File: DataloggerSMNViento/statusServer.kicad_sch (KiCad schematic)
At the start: 15 parts

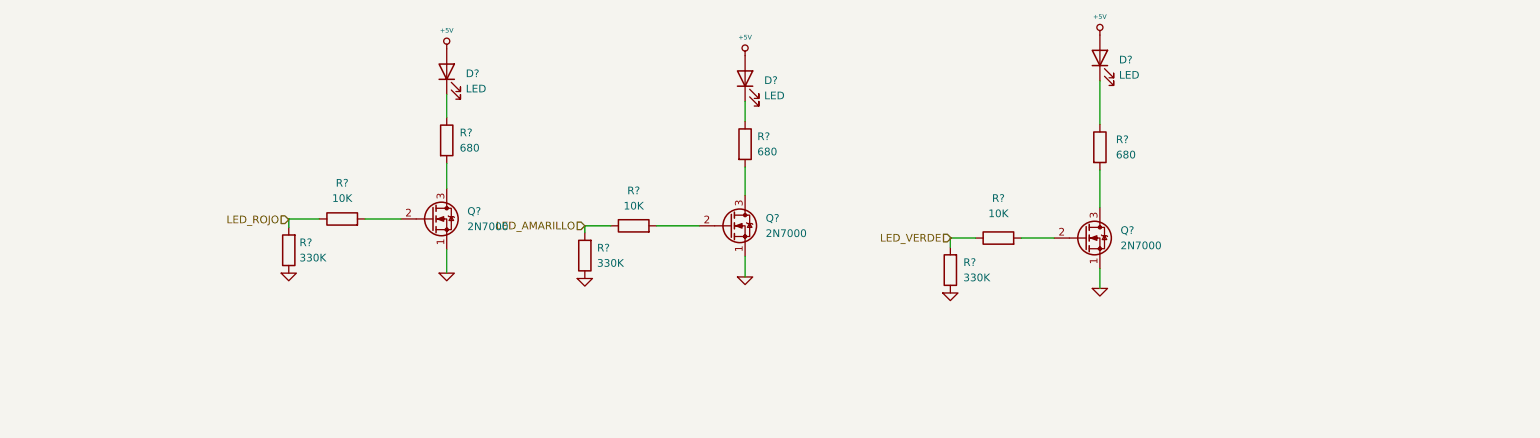
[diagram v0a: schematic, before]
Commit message: Agrego modificaciones al poncho de la EDU CIAA, también agrego una simulacion del circuito para tomar la tensión del ADC del tunnel
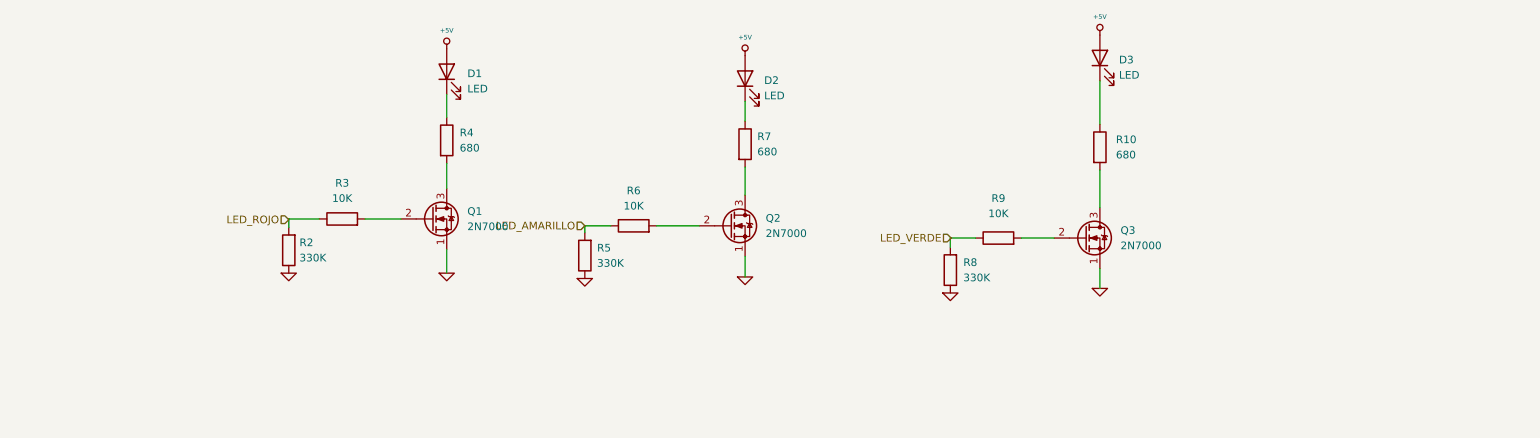
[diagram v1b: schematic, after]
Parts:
- D1, D2, D3: renamed from D?; footprint (none) -> LED_THT:LED_D3.0mm
- R10, R2, R3, R4, R5, R6, R7, R8, R9: renamed from R?; footprint (none) -> Resistor_THT:R_Axial_DIN0207_L6.3mm_D2.5mm_P15.24mm_Horizontal
- gave numbers to parts that had none: 3
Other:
- company: (none) -> Servicio Meteorológico Nacional - FIUBA - UBA
- title: (none) -> Datalogger para SCTV

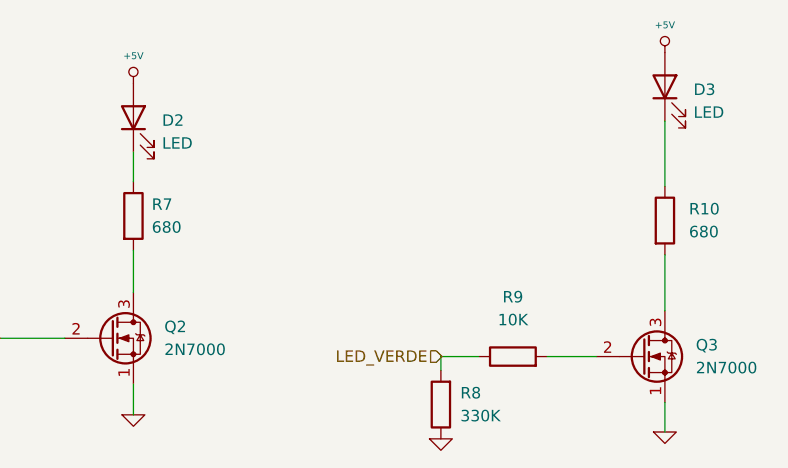
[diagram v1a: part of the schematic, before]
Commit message: Subo la version v1.0 del PCB del poncho de la tesis
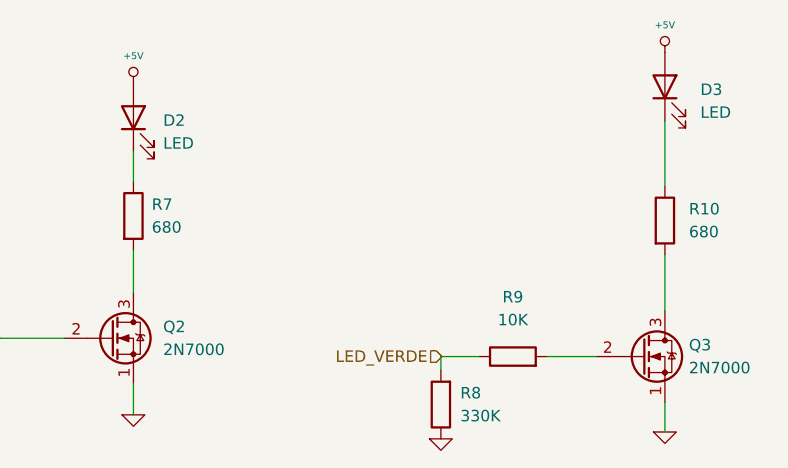
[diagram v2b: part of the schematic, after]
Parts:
- D1, D2, D3: footprint LED_THT:LED_D3.0mm -> LED_SMD:LED_1206_3216Metric
- Q1, Q2, Q3: footprint Package_TO_SOT_THT:TO-92_Inline -> Package_TO_SOT_SMD:SOT-23
- R10, R2, R3, R4, R5, R6, R7, R8, R9: footprint Resistor_THT:R_Axial_DIN0207_L6.3mm_D2.5mm_P15.24mm_Horizontal -> Resistor_SMD:R_1206_3216Metric
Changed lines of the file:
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@@
       (effects (font (size 1.27 1.27)) (justify left))
     )
-    (property "Footprint" "Package_TO_SOT_THT:TO-92_Inline" (id 2) (at 96.901 58.674 0)
+    (property "Footprint" "Package_TO_SOT_SMD:SOT-23" (id 2) (at 96.901 58.674 0)
       (effects (font (size 1.27 1.27) italic) (justify left) hide)
     )
@@
       (effects (font (size 1.27 1.27)) (justify right))
     )
-    (property "Footprint" "Resistor_THT:R_Axial_DIN0207_L6.3mm_D2.5mm_P15.24mm_Horizontal" (id 2) (at 179.959 65.278 90)
+    (property "Footprint" "Resistor_SMD:R_1206_3216Metric" (id 2) (at 179.959 65.278 90)
       (effects (font (size 1.27 1.27)) hide)
     )
@@
       (effects (font (size 1.27 1.27)) (justify left))
     )
-    (property "Footprint" "Resistor_THT:R_Axial_DIN0207_L6.3mm_D2.5mm_P15.24mm_Horizontal" (id 2) (at 201.295 44.831 90)
+    (property "Footprint" "Resistor_SMD:R_1206_3216Metric" (id 2) (at 201.295 44.831 90)
       (effects (font (size 1.27 1.27)) hide)
     )
@@
   (symbol (lib_id "Device:LED") (at 203.073 29.972 90) (unit 1)
     (in_bom yes) (on_board yes) (fields_autoplaced)
-    (property "Reference" "D3" (id 0) (at 206.248 30.2894 90)
-      (effects (font (size 1.27 1.27)) (justify right))
-    )
-    (property "Value" "LED" (id 1) (at 206.248 32.8294 90)
-      (effects (font (size 1.27 1.27)) (justify right))
-    )
-    (property "Footprint" "LED_THT:LED_D3.0mm" (id 2) (at 203.073 29.972 0)
+    (property "Reference" "D3" (id 0) (at 207.01 30.2894 90)
+      (effects (font (size 1.27 1.27)) (justify right))
+    )
+    (property "Value" "LED" (id 1) (at 207.01 32.8294 90)
+      (effects (font (size 1.27 1.27)) (justify right))
+    )
+    (property "Footprint" "LED_SMD:LED_1206_3216Metric" (id 2) (at 203.073 29.972 0)
       (effects (font (size 1.27 1.27)) hide)
     )
@@
       (effects (font (size 1.27 1.27)) (justify left))
     )
-    (property "Footprint" "Resistor_THT:R_Axial_DIN0207_L6.3mm_D2.5mm_P15.24mm_Horizontal" (id 2) (at 142.24 44.323 90)
+    (property "Footprint" "Resistor_SMD:R_1206_3216Metric" (id 2) (at 142.24 44.323 90)
       (effects (font (size 1.27 1.27)) hide)
     )
@@
       (effects (font (size 1.27 1.27)) (justify right))
     )
-    (property "Footprint" "LED_THT:LED_D3.0mm" (id 2) (at 94.361 32.258 0)
+    (property "Footprint" "LED_SMD:LED_1206_3216Metric" (id 2) (at 94.361 32.258 0)
       (effects (font (size 1.27 1.27)) hide)
     )
@@
     (property "Reference" "R3" (id 0) (at 76.962 50.8 90))
     (property "Value" "10K" (id 1) (at 76.962 53.34 90))
-    (property "Footprint" "Resistor_THT:R_Axial_DIN0207_L6.3mm_D2.5mm_P15.24mm_Horizontal" (id 2) (at 76.962 58.547 90)
+    (property "Footprint" "Resistor_SMD:R_1206_3216Metric" (id 2) (at 76.962 58.547 90)
       (effects (font (size 1.27 1.27)) hide)
     )
@@
   (symbol (lib_id "Transistor_FET:2N7000") (at 200.533 59.944 0) (unit 1)
     (in_bom yes) (on_board yes) (fields_autoplaced)
-    (property "Reference" "Q3" (id 0) (at 206.502 58.6739 0)
-      (effects (font (size 1.27 1.27)) (justify left))
-    )
-    (property "Value" "2N7000" (id 1) (at 206.502 61.2139 0)
-      (effects (font (size 1.27 1.27)) (justify left))
-    )
-    (property "Footprint" "Package_TO_SOT_THT:TO-92_Inline" (id 2) (at 205.613 61.849 0)
+    (property "Reference" "Q3" (id 0) (at 205.74 58.6739 0)
+      (effects (font (size 1.27 1.27)) (justify left))
+    )
+    (property "Value" "2N7000" (id 1) (at 205.74 61.2139 0)
+      (effects (font (size 1.27 1.27)) (justify left))
+    )
+    (property "Footprint" "Package_TO_SOT_SMD:SOT-23" (id 2) (at 205.613 61.849 0)
       (effects (font (size 1.27 1.27) italic) (justify left) hide)
     )
@@
       (effects (font (size 1.27 1.27)) (justify right))
     )
-    (property "Footprint" "Resistor_THT:R_Axial_DIN0207_L6.3mm_D2.5mm_P15.24mm_Horizontal" (id 2) (at 119.126 62.865 90)
+    (property "Footprint" "Resistor_SMD:R_1206_3216Metric" (id 2) (at 119.126 62.865 90)
       (effects (font (size 1.27 1.27)) hide)
     )
@@
     (property "Reference" "R6" (id 0) (at 125.476 52.07 90))
     (property "Value" "10K" (id 1) (at 125.476 54.61 90))
-    (property "Footprint" "Resistor_THT:R_Axial_DIN0207_L6.3mm_D2.5mm_P15.24mm_Horizontal" (id 2) (at 125.476 59.69 90)
+    (property "Footprint" "Resistor_SMD:R_1206_3216Metric" (id 2) (at 125.476 59.69 90)
       (effects (font (size 1.27 1.27)) hide)
     )
@@
   (symbol (lib_id "Transistor_FET:2N7000") (at 141.478 57.912 0) (unit 1)
     (in_bom yes) (on_board yes) (fields_autoplaced)
-    (property "Reference" "Q2" (id 0) (at 147.447 56.6419 0)
-      (effects (font (size 1.27 1.27)) (justify left))
-    )
-    (property "Value" "2N7000" (id 1) (at 147.447 59.1819 0)
-      (effects (font (size 1.27 1.27)) (justify left))
-    )
-    (property "Footprint" "Package_TO_SOT_THT:TO-92_Inline" (id 2) (at 146.558 59.817 0)
+    (property "Reference" "Q2" (id 0) (at 147.32 56.6419 0)
+      (effects (font (size 1.27 1.27)) (justify left))
+    )
+    (property "Value" "2N7000" (id 1) (at 147.32 59.1819 0)
+      (effects (font (size 1.27 1.27)) (justify left))
+    )
+    (property "Footprint" "Package_TO_SOT_SMD:SOT-23" (id 2) (at 146.558 59.817 0)
       (effects (font (size 1.27 1.27) italic) (justify left) hide)
     )
@@
       (effects (font (size 1.27 1.27)) (justify left))
     )
-    (property "Footprint" "Resistor_THT:R_Axial_DIN0207_L6.3mm_D2.5mm_P15.24mm_Horizontal" (id 2) (at 92.583 43.688 90)
+    (property "Footprint" "Resistor_SMD:R_1206_3216Metric" (id 2) (at 92.583 43.688 90)
       (effects (font (size 1.27 1.27)) hide)
     )
@@
     (property "Reference" "R9" (id 0) (at 186.182 53.34 90))
     (property "Value" "10K" (id 1) (at 186.182 55.88 90))
-    (property "Footprint" "Resistor_THT:R_Axial_DIN0207_L6.3mm_D2.5mm_P15.24mm_Horizontal" (id 2) (at 186.182 61.722 90)
+    (property "Footprint" "Resistor_SMD:R_1206_3216Metric" (id 2) (at 186.182 61.722 90)
       (effects (font (size 1.27 1.27)) hide)
     )
@@
       (effects (font (size 1.27 1.27)) (justify right))
     )
-    (property "Footprint" "Resistor_THT:R_Axial_DIN0207_L6.3mm_D2.5mm_P15.24mm_Horizontal" (id 2) (at 69.85 61.976 90)
+    (property "Footprint" "Resistor_SMD:R_1206_3216Metric" (id 2) (at 69.85 61.976 90)
       (effects (font (size 1.27 1.27)) hide)
     )
@@
   (symbol (lib_id "Device:LED") (at 144.018 33.401 90) (unit 1)
     (in_bom yes) (on_board yes) (fields_autoplaced)
-    (property "Reference" "D2" (id 0) (at 147.193 33.7184 90)
-      (effects (font (size 1.27 1.27)) (justify right))
-    )
-    (property "Value" "LED" (id 1) (at 147.193 36.2584 90)
-      (effects (font (size 1.27 1.27)) (justify right))
-    )
-    (property "Footprint" "LED_THT:LED_D3.0mm" (id 2) (at 144.018 33.401 0)
-      (effects (font (size 1.27 1.27)) hide)
-    )
+    (property "Reference" "D2" (id 0) (at 147.32 33.7184 90)
+      (effects (font (size 1.27 1.27)) (justify right))
+    )
+    (property "Value" "LED" (id 1) (at 147.32 36.2584 90)
+      (effects (font (size 1.27 1.27)) (justify right))
+    )
+    (property "Footprint" "LED_SMD:LED_1206_3216Metric" (id 2) (at 144.018 33.401 0)
+      (effects (font (size 1.27 1.27)) hide)
+    )

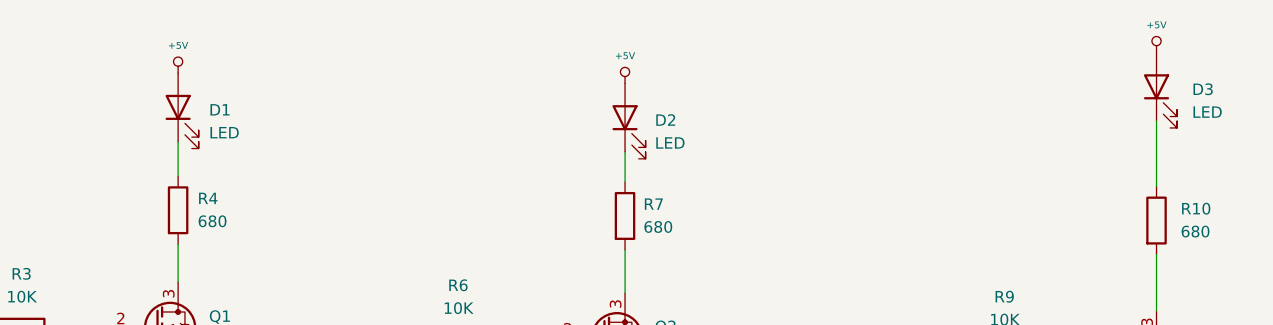
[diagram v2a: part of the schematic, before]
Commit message: Se cambio la alimentacion de los modulos por el stepDown
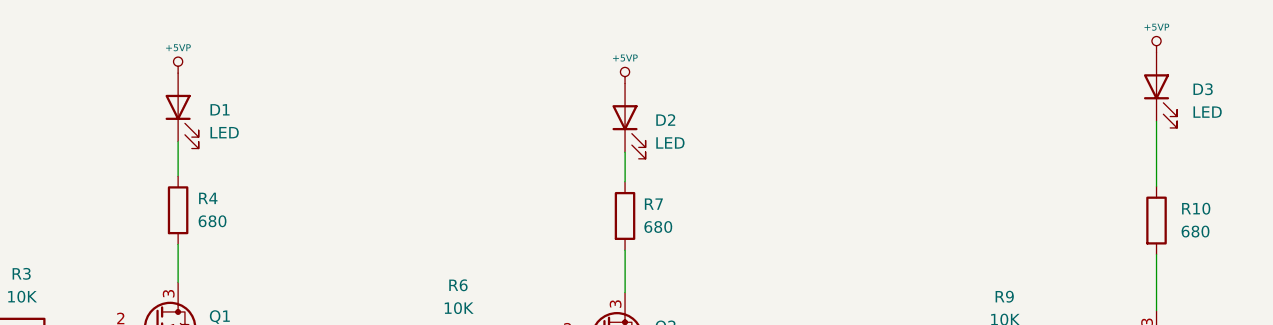
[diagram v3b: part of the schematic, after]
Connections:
- net +5V renamed +5VP
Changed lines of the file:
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@@
     (effects (font (size 1.27 1.27)) (justify right))
-  )
-  (symbol (lib_id "Misc_Poncho_Grande:+5V") (at 94.361 28.448 0) (unit 1)
-    (in_bom yes) (on_board yes) (fields_autoplaced)
-    (property "Reference" "#PWR016" (id 0) (at 94.361 26.162 0)
-      (effects (font (size 0.508 0.508)) hide)
-    )
-    (property "Value" "+5V" (id 1) (at 94.361 25.4 0)
-      (effects (font (size 0.762 0.762)))
-    )
-    (property "Footprint" "" (id 2) (at 94.361 28.448 0)
-      (effects (font (size 1.524 1.524)))
-    )
-    (property "Datasheet" "" (id 3) (at 94.361 28.448 0)
-      (effects (font (size 1.524 1.524)))
-    )
-    (pin "1")
   )
   (symbol (lib_id "Transistor_FET:2N7000") (at 91.821 56.769 0) (unit 1)
@@
     (pin "3")
   )
+  (symbol (lib_id "Misc_Poncho_Grande:+5VP") (at 203.073 26.162 0) (unit 1)
+    (in_bom yes) (on_board yes) (fields_autoplaced)
+    (property "Reference" "#PWR016" (id 0) (at 203.073 23.876 0)
+      (effects (font (size 0.508 0.508)) hide)
+    )
+    (property "Value" "+5VP" (id 1) (at 203.073 23.368 0)
+      (effects (font (size 0.762 0.762)))
+    )
+    (property "Footprint" "" (id 2) (at 203.073 26.162 0)
+      (effects (font (size 1.524 1.524)))
+    )
+    (property "Datasheet" "" (id 3) (at 203.073 26.162 0)
+      (effects (font (size 1.524 1.524)))
+    )
+    (pin "1")
+  )
   (symbol (lib_id "Misc_Poncho_Grande:GND") (at 68.072 65.786 0) (unit 1)
     (in_bom yes) (on_board yes) (fields_autoplaced)
@@
     (pin "1")
   )
-  (symbol (lib_id "Misc_Poncho_Grande:+5V") (at 203.073 26.162 0) (unit 1)
-    (in_bom yes) (on_board yes) (fields_autoplaced)
-    (property "Reference" "#PWR022" (id 0) (at 203.073 23.876 0)
+  (symbol (lib_id "Device:R") (at 178.181 65.278 180) (unit 1)
+    (in_bom yes) (on_board yes) (fields_autoplaced)
+    (property "Reference" "R8" (id 0) (at 180.34 64.0079 0)
+      (effects (font (size 1.27 1.27)) (justify right))
+    )
+    (property "Value" "330K" (id 1) (at 180.34 66.5479 0)
+      (effects (font (size 1.27 1.27)) (justify right))
+    )
+    (property "Footprint" "Resistor_SMD:R_1206_3216Metric" (id 2) (at 179.959 65.278 90)
+      (effects (font (size 1.27 1.27)) hide)
+    )
+    (property "Datasheet" "~" (id 3) (at 178.181 65.278 0)
+      (effects (font (size 1.27 1.27)) hide)
+    )
+    (pin "1")
+    (pin "2")
+  )
+  (symbol (lib_id "Device:R") (at 203.073 44.831 0) (unit 1)
+    (in_bom yes) (on_board yes) (fields_autoplaced)
+    (property "Reference" "R10" (id 0) (at 205.74 43.5609 0)
+      (effects (font (size 1.27 1.27)) (justify left))
+    )
+    (property "Value" "680" (id 1) (at 205.74 46.1009 0)
+      (effects (font (size 1.27 1.27)) (justify left))
+    )
+    (property "Footprint" "Resistor_SMD:R_1206_3216Metric" (id 2) (at 201.295 44.831 90)
+      (effects (font (size 1.27 1.27)) hide)
+    )
+    (property "Datasheet" "~" (id 3) (at 203.073 44.831 0)
+      (effects (font (size 1.27 1.27)) hide)
+    )
+    (pin "1")
+    (pin "2")
+  )
+  (symbol (lib_id "Device:LED") (at 203.073 29.972 90) (unit 1)
+    (in_bom yes) (on_board yes) (fields_autoplaced)
+    (property "Reference" "D3" (id 0) (at 207.01 30.2894 90)
+      (effects (font (size 1.27 1.27)) (justify right))
+    )
+    (property "Value" "LED" (id 1) (at 207.01 32.8294 90)
+      (effects (font (size 1.27 1.27)) (justify right))
+    )
+    (property "Footprint" "LED_SMD:LED_1206_3216Metric" (id 2) (at 203.073 29.972 0)
+      (effects (font (size 1.27 1.27)) hide)
+    )
+    (property "Datasheet" "~" (id 3) (at 203.073 29.972 0)
+      (effects (font (size 1.27 1.27)) hide)
+    )
+    (pin "1")
+    (pin "2")
+  )
+  (symbol (lib_id "Misc_Poncho_Grande:+5VP") (at 144.018 29.591 0) (unit 1)
+    (in_bom yes) (on_board yes) (fields_autoplaced)
+    (property "Reference" "#PWR014" (id 0) (at 144.018 27.305 0)
       (effects (font (size 0.508 0.508)) hide)
     )
-    (property "Value" "+5V" (id 1) (at 203.073 23.114 0)
+    (property "Value" "+5VP" (id 1) (at 144.018 26.797 0)
       (effects (font (size 0.762 0.762)))
     )
-    (property "Footprint" "" (id 2) (at 203.073 26.162 0)
-      (effects (font (size 1.524 1.524)))
-    )
-    (property "Datasheet" "" (id 3) (at 203.073 26.162 0)
-      (effects (font (size 1.524 1.524)))
-    )
-    (pin "1")
-  )
-  (symbol (lib_id "Device:R") (at 178.181 65.278 180) (unit 1)
-    (in_bom yes) (on_board yes) (fields_autoplaced)
-    (property "Reference" "R8" (id 0) (at 180.34 64.0079 0)
-      (effects (font (size 1.27 1.27)) (justify right))
-    )
-    (property "Value" "330K" (id 1) (at 180.34 66.5479 0)
-      (effects (font (size 1.27 1.27)) (justify right))
-    )
-    (property "Footprint" "Resistor_SMD:R_1206_3216Metric" (id 2) (at 179.959 65.278 90)
-      (effects (font (size 1.27 1.27)) hide)
-    )
-    (property "Datasheet" "~" (id 3) (at 178.181 65.278 0)
-      (effects (font (size 1.27 1.27)) hide)
-    )
-    (pin "1")
-    (pin "2")
-  )
-  (symbol (lib_id "Device:R") (at 203.073 44.831 0) (unit 1)
-    (in_bom yes) (on_board yes) (fields_autoplaced)
-    (property "Reference" "R10" (id 0) (at 205.74 43.5609 0)
-      (effects (font (size 1.27 1.27)) (justify left))
-    )
-    (property "Value" "680" (id 1) (at 205.74 46.1009 0)
-      (effects (font (size 1.27 1.27)) (justify left))
-    )
-    (property "Footprint" "Resistor_SMD:R_1206_3216Metric" (id 2) (at 201.295 44.831 90)
-      (effects (font (size 1.27 1.27)) hide)
-    )
-    (property "Datasheet" "~" (id 3) (at 203.073 44.831 0)
-      (effects (font (size 1.27 1.27)) hide)
-    )
-    (pin "1")
-    (pin "2")
-  )
-  (symbol (lib_id "Device:LED") (at 203.073 29.972 90) (unit 1)
-    (in_bom yes) (on_board yes) (fields_autoplaced)
-    (property "Reference" "D3" (id 0) (at 207.01 30.2894 90)
-      (effects (font (size 1.27 1.27)) (justify right))
-    )
-    (property "Value" "LED" (id 1) (at 207.01 32.8294 90)
-      (effects (font (size 1.27 1.27)) (justify right))
-    )
-    (property "Footprint" "LED_SMD:LED_1206_3216Metric" (id 2) (at 203.073 29.972 0)
-      (effects (font (size 1.27 1.27)) hide)
-    )
-    (property "Datasheet" "~" (id 3) (at 203.073 29.972 0)
-      (effects (font (size 1.27 1.27)) hide)
-    )
-    (pin "1")
-    (pin "2")
+    (property "Footprint" "" (id 2) (at 144.018 29.591 0)
+      (effects (font (size 1.524 1.524)))
+    )
+    (property "Datasheet" "" (id 3) (at 144.018 29.591 0)
+      (effects (font (size 1.524 1.524)))
+    )
+    (pin "1")
   )
   (symbol (lib_id "Device:R") (at 144.018 44.323 0) (unit 1)
@@
     (pin "2")
   )
-  (symbol (lib_id "Misc_Poncho_Grande:+5V") (at 144.018 29.591 0) (unit 1)
-    (in_bom yes) (on_board yes) (fields_autoplaced)
-    (property "Reference" "#PWR019" (id 0) (at 144.018 27.305 0)
-      (effects (font (size 0.508 0.508)) hide)
-    )
-    (property "Value" "+5V" (id 1) (at 144.018 26.543 0)
-      (effects (font (size 0.762 0.762)))
-    )
-    (property "Footprint" "" (id 2) (at 144.018 29.591 0)
-      (effects (font (size 1.524 1.524)))
-    )
-    (property "Datasheet" "" (id 3) (at 144.018 29.591 0)
-      (effects (font (size 1.524 1.524)))
-    )
-    (pin "1")
-  )
   (symbol (lib_id "Misc_Poncho_Grande:GND") (at 144.018 66.421 0) (unit 1)
     (in_bom yes) (on_board yes) (fields_autoplaced)
@@
     (pin "2")
   )
+  (symbol (lib_id "Misc_Poncho_Grande:+5VP") (at 94.361 28.448 0) (unit 1)
+    (in_bom yes) (on_board yes) (fields_autoplaced)
+    (property "Reference" "#PWR0103" (id 0) (at 94.361 26.162 0)
+      (effects (font (size 0.508 0.508)) hide)
+    )
+    (property "Value" "+5VP" (id 1) (at 94.361 25.654 0)
+      (effects (font (size 0.762 0.762)))
+    )
+    (property "Footprint" "" (id 2) (at 94.361 28.448 0)
+      (effects (font (size 1.524 1.524)))
+    )
+    (property "Datasheet" "" (id 3) (at 94.361 28.448 0)
+      (effects (font (size 1.524 1.524)))
+    )
+    (pin "1")
+  )
 )
